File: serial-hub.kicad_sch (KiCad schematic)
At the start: 41 parts, among them J1 USB_C_Receptacle_USB2.0, J2 RJ45, J3 RJ45, J4 RJ45, J5 RJ45, U1 CH344, U2 MAX232, U3 AMS1117-3.3, U4 MAX232, U5 MAX232, U6 MAX232, Y1 8MHz

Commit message: init pcb design
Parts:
- removed C1: C, symbol Device:C
- added D1: 0, Diode_SMD:D_SOD-123, symbol Device:D
- added R3: 2, Resistor_SMD:R_0603_1608Metric, symbol Device:R
- added R4: 4.7k, Resistor_SMD:R_0402_1005Metric, symbol Device:R
- C1: renamed from C10; footprint (none) -> Capacitor_SMD:C_0603_1608Metric
- C10: renamed from C14; value 0.1uF -> 1uF; footprint (none) -> Capacitor_SMD:C_0402_1005Metric
- C11: renamed from C7; value 0.1uF -> 1uF; footprint (none) -> Capacitor_SMD:C_0402_1005Metric
- C12: renamed from C17; value 0.1uF -> 1uF; footprint (none) -> Capacitor_SMD:C_0402_1005Metric
- C13: renamed from C8; value 0.1uF -> 1uF; footprint (none) -> Capacitor_SMD:C_0402_1005Metric
- C14: renamed from C9; value 0.1uF -> 1uF; footprint (none) -> Capacitor_SMD:C_0402_1005Metric
- C15: renamed from C20; value 0.1uF -> 1uF; footprint (none) -> Capacitor_SMD:C_0402_1005Metric
- C16: renamed from C21; value 0.1uF -> 1uF; footprint (none) -> Capacitor_SMD:C_0402_1005Metric
- C17: renamed from C15; value 0.1uF -> 1uF; footprint (none) -> Capacitor_SMD:C_0402_1005Metric
- C18: renamed from C16; value 0.1uF -> 1uF; footprint (none) -> Capacitor_SMD:C_0402_1005Metric
- C19: renamed from C18; value 0.1uF -> 1uF; footprint (none) -> Capacitor_SMD:C_0402_1005Metric
- C2: footprint (none) -> Capacitor_SMD:C_0402_1005Metric
- C20: renamed from C19; value 0.1uF -> 1uF; footprint (none) -> Capacitor_SMD:C_0402_1005Metric
- C21: renamed from C22; value 0.1uF -> 1uF; footprint (none) -> Capacitor_SMD:C_0402_1005Metric
- C22: renamed from C23; value 0.1uF -> 1uF; footprint (none) -> Capacitor_SMD:C_0402_1005Metric
- C23: renamed from C24; value 0.1uF -> 1uF; footprint (none) -> Capacitor_SMD:C_0402_1005Metric
- C24: renamed from C25; value 0.1uF -> 1uF; footprint (none) -> Capacitor_SMD:C_0402_1005Metric
- C3: renamed from C11; footprint (none) -> Capacitor_SMD:C_0402_1005Metric
- C4: renamed from C12; footprint (none) -> Capacitor_SMD:C_0402_1005Metric
- C5: renamed from C13; value 10uF -> 22uF; footprint (none) -> Capacitor_SMD:C_0603_1608Metric
- C6: renamed from C3; footprint (none) -> Capacitor_SMD:C_0402_1005Metric
- C7: renamed from C4; footprint (none) -> Capacitor_SMD:C_0402_1005Metric
- C8: renamed from C5; value C -> 0.1uF; footprint (none) -> Capacitor_SMD:C_0402_1005Metric
- C9: renamed from C6; value 0.1uF -> 1uF; footprint (none) -> Capacitor_SMD:C_0402_1005Metric
- R1: renamed from R2; footprint (none) -> Resistor_SMD:R_0402_1005Metric
- R2: renamed from R3; footprint (none) -> Resistor_SMD:R_0402_1005Metric
- R5: renamed from R1; footprint (none) -> Resistor_SMD:R_0402_1005Metric
- R6: renamed from R4; footprint (none) -> Resistor_SMD:R_0402_1005Metric
- U3: renamed from U2; footprint (none) -> Package_SO:SOIC-16_3.9x9.9mm_P1.27mm
- U4, U5, U6: footprint (none) -> Package_SO:SOIC-16_3.9x9.9mm_P1.27mm
- Y1: footprint (none) -> Crystal:Crystal_SMD_5032-2Pin_5.0x3.2mm
- renumbered U3 to U2
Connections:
- net +3.3V: now also R3.1; no longer C5.1
- net C0_RX: no longer U1.13 (RXD1)
- net C1_RX: now also U1.13 (RXD1)
- net GND: now also U2.1 (GND), R4.2
- net VBUS: now also D1.1 (K); no longer J1.A4 (VBUS), J1.A9 (VBUS), J1.B4 (VBUS), J1.B9 (VBUS)
- net RTS3: now reaches U1.45 (RTS3/GPIO7)
- net RTS3: now also R4.1
- new net: D1.2 (A), J1.A4 (VBUS), J1.A9 (VBUS), J1.B4 (VBUS), J1.B9 (VBUS)
- new net: C5.1, R3.2
- no-connect marks 18 -> 17
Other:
- moved on the sheet: C10, C11, C12, C13, C14, C15, C16, C17, C18, C19, C20, C21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

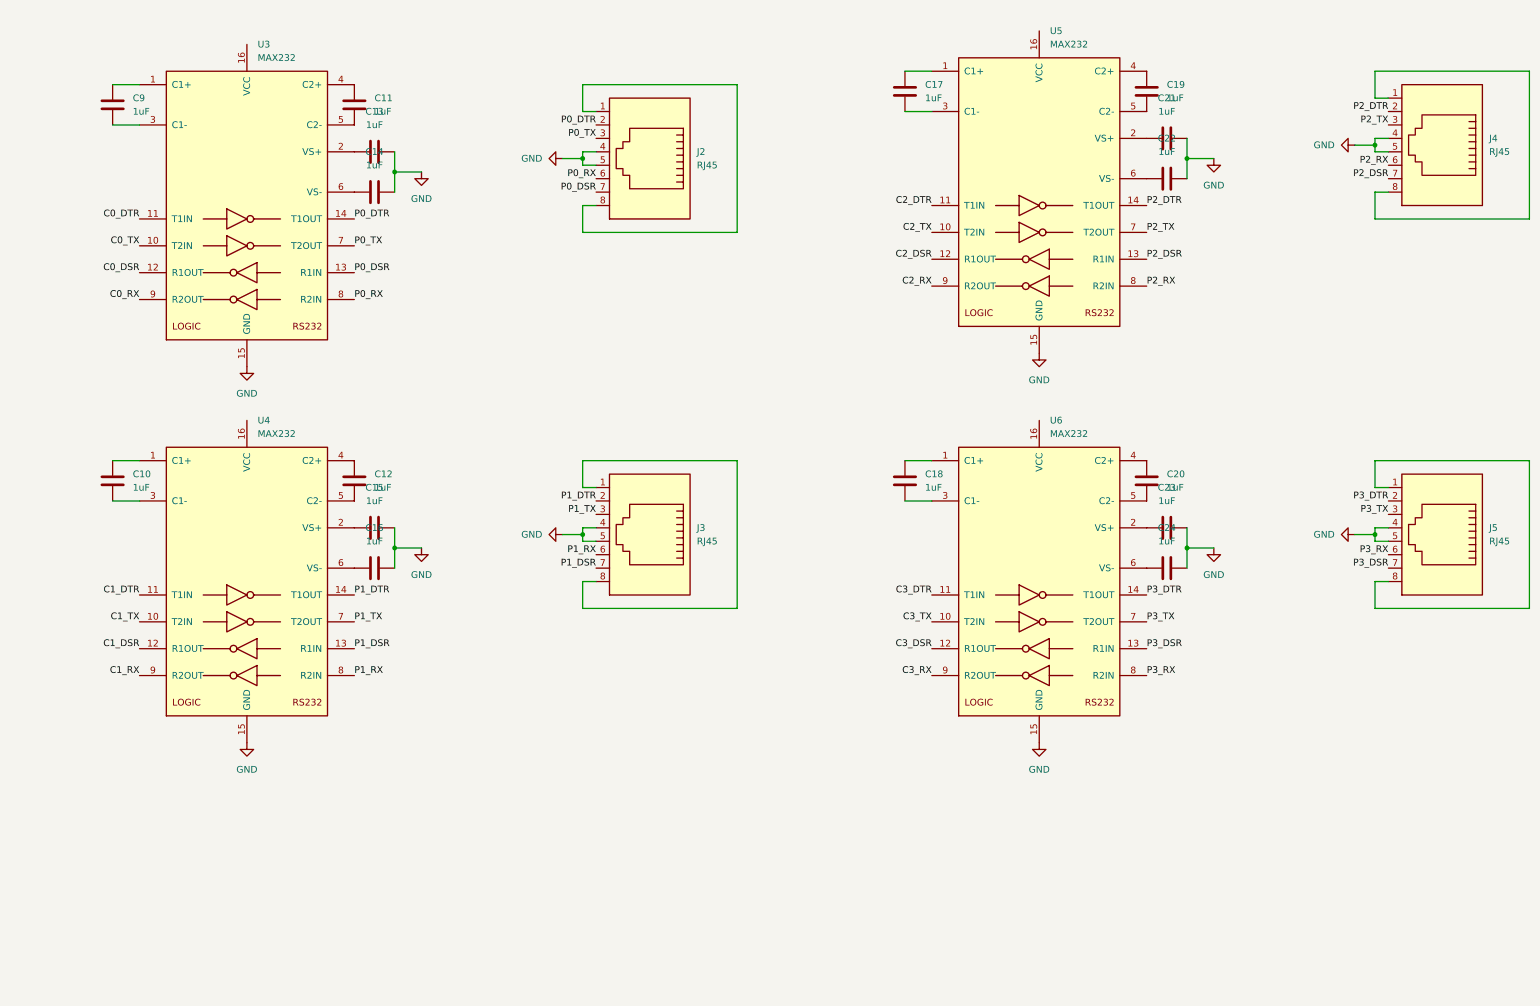
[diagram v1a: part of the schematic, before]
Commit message: fix max232 caps
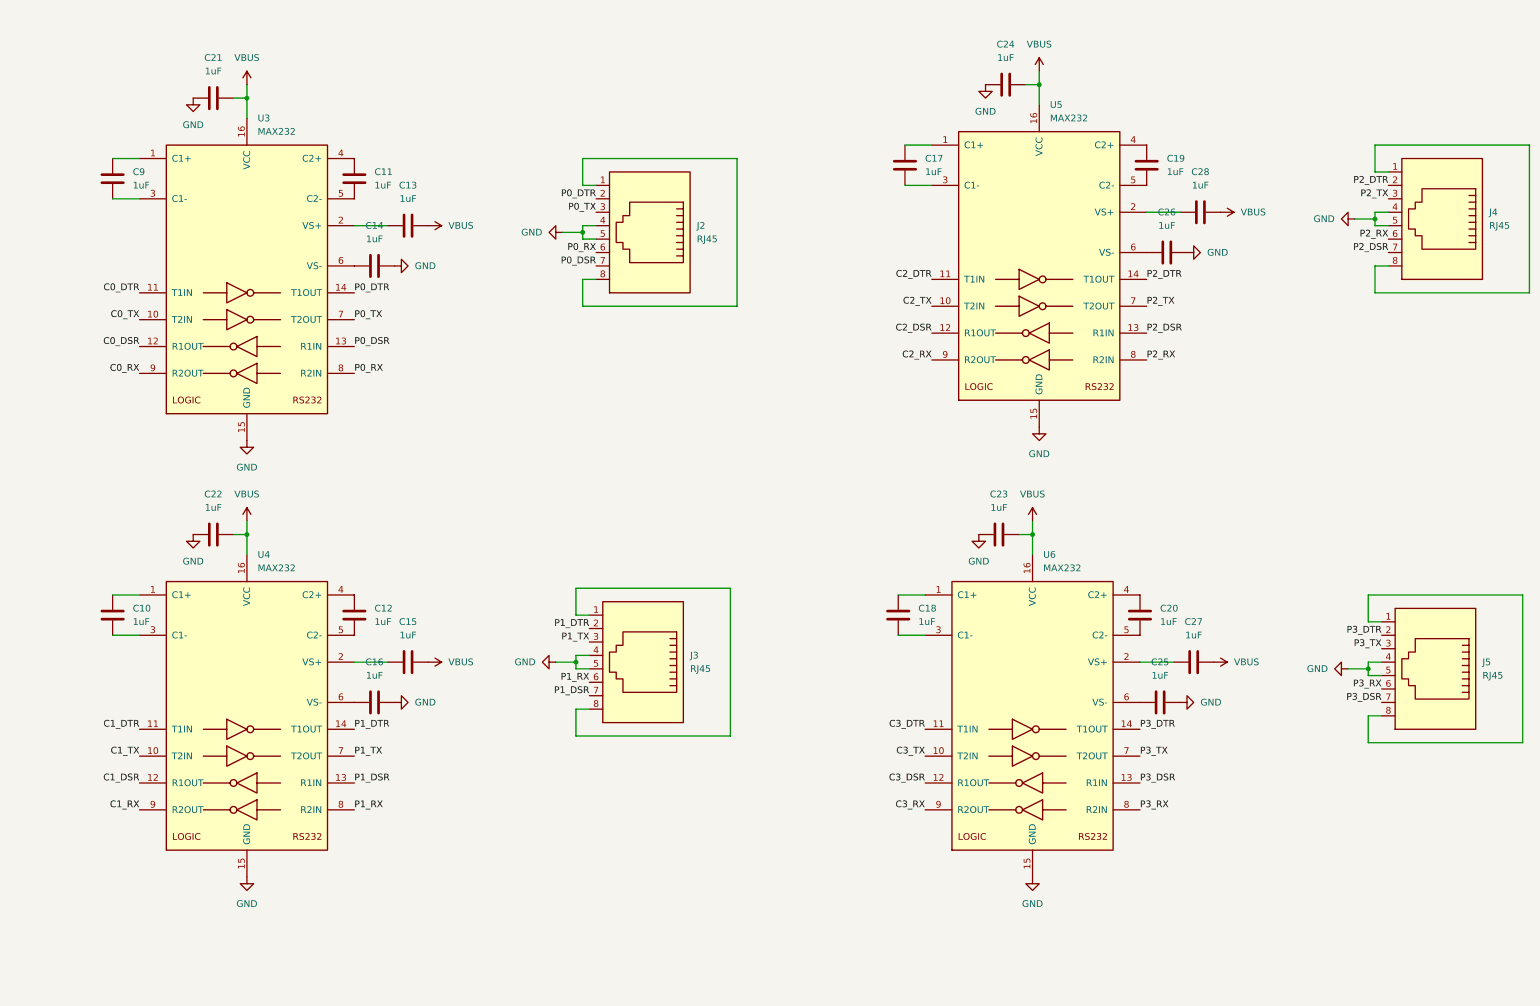
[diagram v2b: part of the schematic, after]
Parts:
- added C25, C26, C27, C28: 1uF, Capacitor_SMD:C_0402_1005Metric, symbol Device:C
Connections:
- net GND: now also C21.1, C22.1, C23.1, C24.1, C25.2, C26.2; no longer C13.2, C15.2, C21.2, C22.2, C23.2, C24.2
- net VBUS: now also C13.2, C15.2, C21.2, C22.2, C23.2, C24.2, U3.16 (VCC), U4.16 (VCC), U5.16 (VCC), U6.16 (VCC), C27.2, C28.2
- net at U5.2 (VS+): now also C28.1; no longer C21.1
- net at U6.2 (VS+): now also C27.1; no longer C23.1
- net at U6.6 (VS-): now also C25.1; no longer C24.1
- net at U5.6 (VS-): now also C26.1; no longer C22.1
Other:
- moved on the sheet: C10, C11, C12, C13, C14, C15, C16, C17, C18, C19, C20, C9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

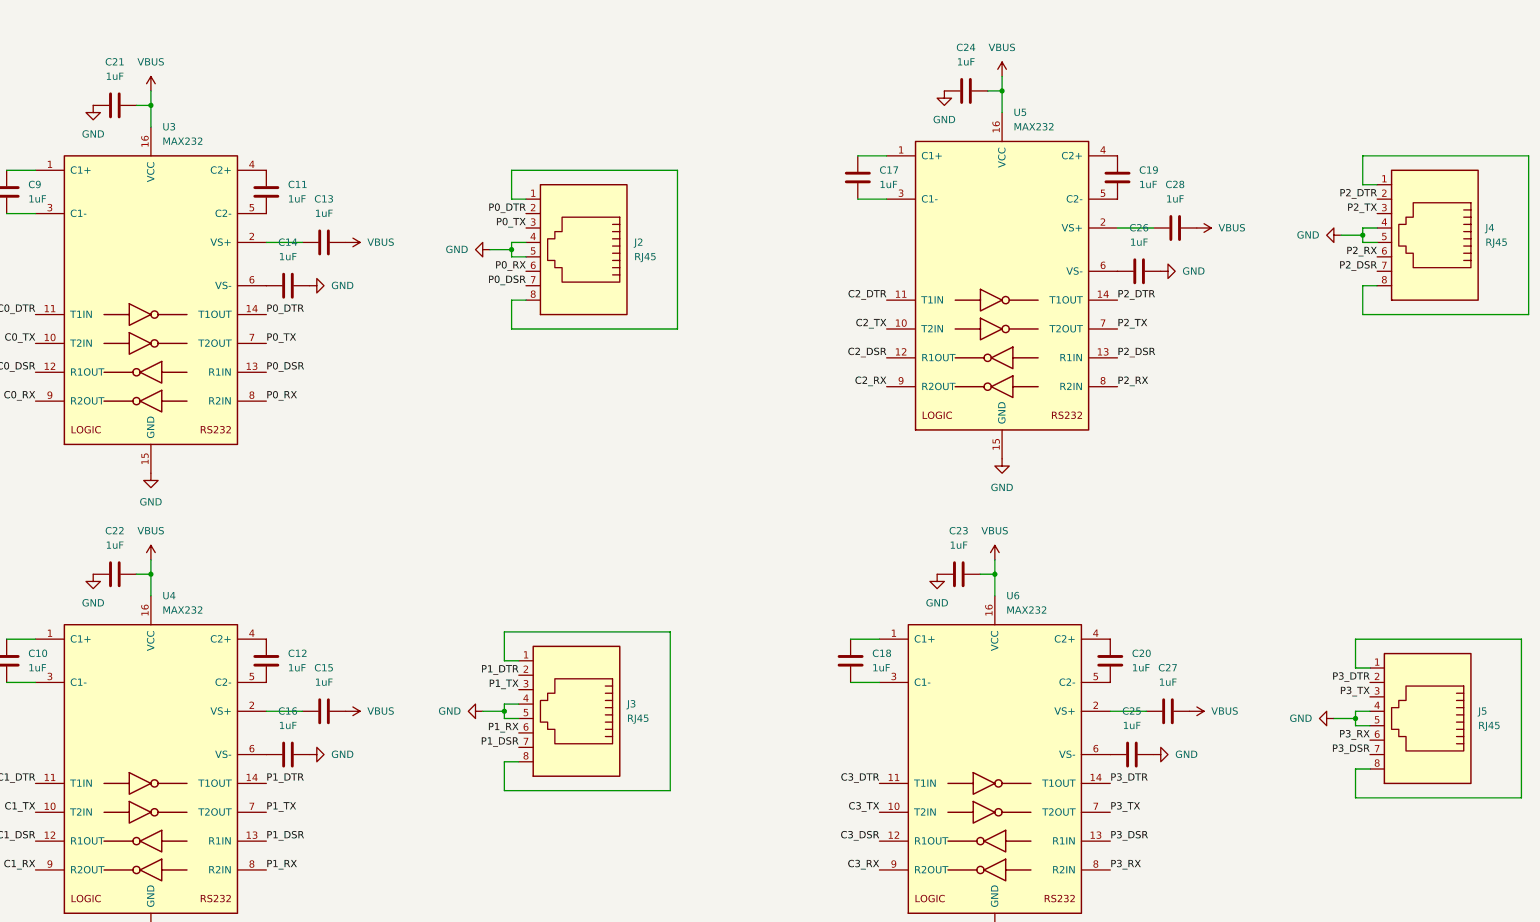
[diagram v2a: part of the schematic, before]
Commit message: update schematic
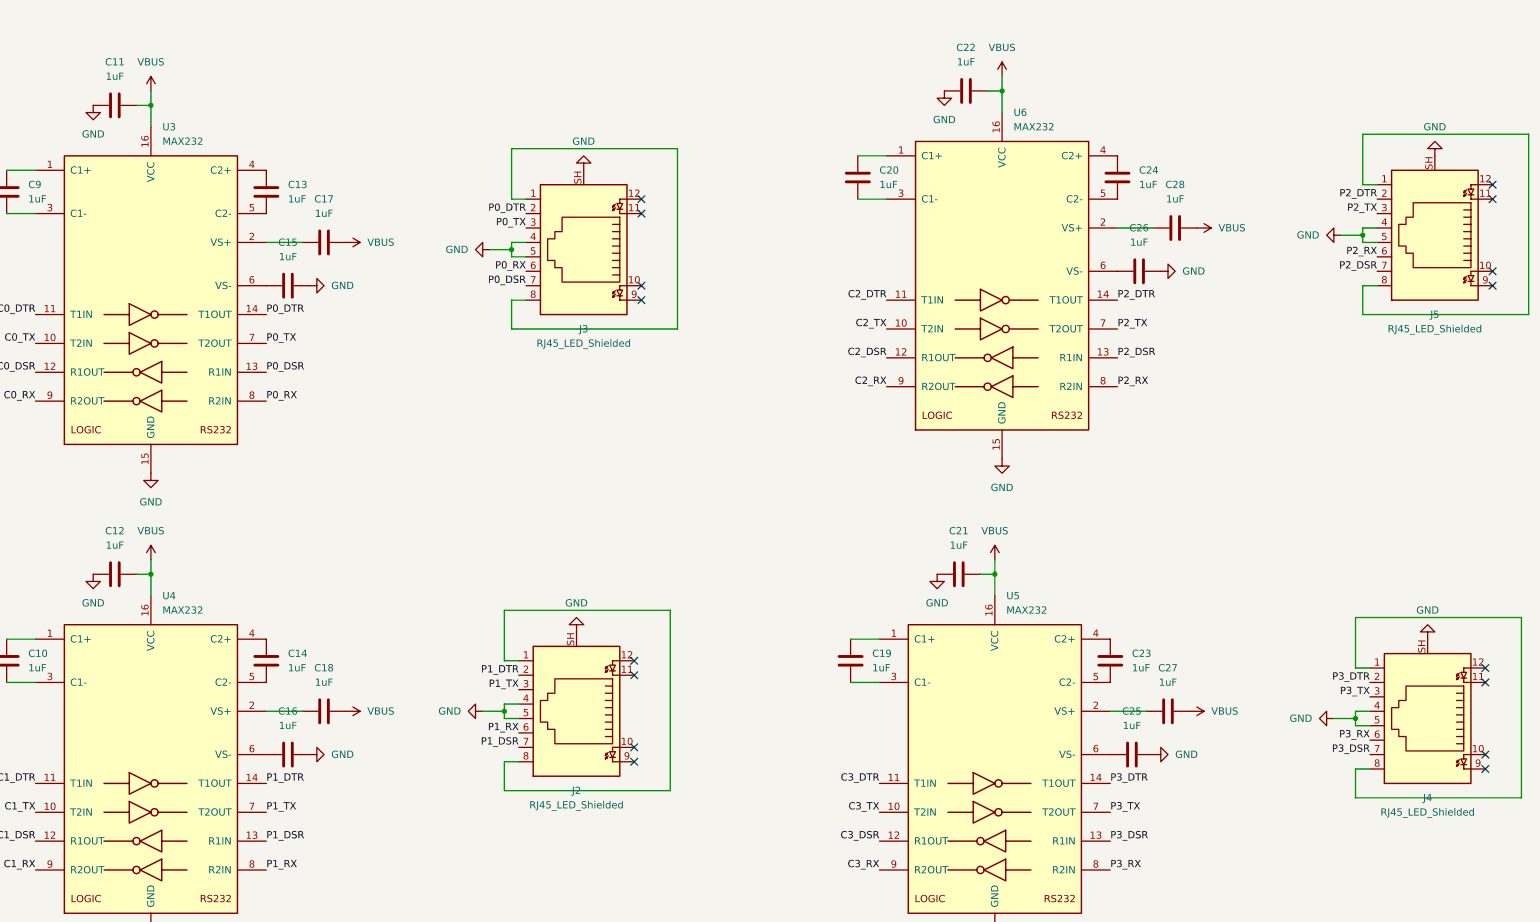
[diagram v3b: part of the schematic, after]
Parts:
- removed J2, J3, J4, J5: RJ45, Connector_RJ:RJ45_Amphenol_RJHSE538X, symbol Connector:RJ45
- added J2, J3, J4, J5: RJ45_LED_Shielded, symbol Connector:RJ45_LED_Shielded
- renumbered C21 to C11, C22 to C12, C11 to C13, C12 to C14, C14 to C15, C13 to C17, C15 to C18, C18 to C19, C17 to C20, C23 to C21, C24 to C22, C20 to C23, C19 to C24, U6 to U5, U5 to U6
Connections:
- net GND: now also J2.4, J2.5, J2.SH, J3.4, J3.5, J3.SH, J4.4, J4.5, J4.SH, J5.4, J5.5, J5.SH
- net P0_DSR: now also J3.7
- net P0_DTR: now also J3.2
- net P0_RX: now also J3.6
- net P0_TX: now also J3.3
- net P1_DSR: now also J2.7
- net P1_DTR: now also J2.2
- net P1_RX: now also J2.6
- net P1_TX: now also J2.3
- net P2_DSR: now also J5.7
- net P2_DTR: now also J5.2
- net P2_RX: now also J5.6
- net P2_TX: now also J5.3
- net P3_DSR: now also J4.7
- net P3_DTR: now also J4.2
- net P3_RX: now also J4.6
- net P3_TX: now also J4.3
- new net: J5.1, J5.8
- new net: J4.1, J4.8
- new net: J2.1, J2.8
- new net: J3.1, J3.8
- no-connect marks 17 -> 33

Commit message: update sch
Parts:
- C10, C11, C12, C13, C14, C15, C16, C17, C18, C19, C2, C20, C21, C22, C23, C24, C25, C26, C27, C28, C3, C4, C8, C9: footprint Capacitor_SMD:C_0402_1005Metric -> Capacitor_SMD:C_0603_1608Metric
- C5: footprint Capacitor_SMD:C_0603_1608Metric -> Capacitor_SMD:C_0805_2012Metric
- C6, C7: footprint Capacitor_SMD:C_0402_1005Metric -> Capacitor_SMD:C_0805_2012Metric
- J2, J3, J4, J5: footprint (none) -> Connector_RJ:RJ45_Hanrun_HR911105A
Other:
- moved on the sheet: C8, R6

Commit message: update PCB
Signed-off-by: David Bauer <mail@david-bauer.net>
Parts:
- C1: LCSC (none) -> C96446
- C10, C11, C12, C13, C14, C15, C16, C17, C18, C19, C20, C21, C22, C23, C24, C25, C26, C27, C28, C9: LCSC (none) -> C15849
- C2, C3, C4, C8: LCSC (none) -> C14663
- C5: LCSC (none) -> C45783
- C6, C7: footprint Capacitor_SMD:C_0805_2012Metric -> Capacitor_SMD:C_0402_1005Metric; LCSC (none) -> C1555
- D1: LCSC (none) -> C8598
- J1: LCSC (none) -> C963413
- J2, J3, J4, J5: LCSC (none) -> C12074
- R1, R2: LCSC (none) -> C17606
- R3: LCSC (none) -> C22977
- R4, R5, R6: LCSC (none) -> C25900
- U1: LCSC (none) -> C2988084
- U2: LCSC (none) -> C6186
- U3, U4, U5, U6: LCSC (none) -> C26860
- Y1: LCSC (none) -> C115962
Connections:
- net C0_DSR: no longer names the net of U3.12 (R1OUT)
- net C0_DSR: no longer U1.29 (DSR0/GPIO14)
- net C0_DTR: no longer names the net of U3.11 (T1IN)
- net C0_DTR: no longer U1.39 (DTR0/TNOW0/GPIO8)
- net C1_DSR: no longer names the net of U4.12 (R1OUT)
- net C1_DSR: no longer U1.17 (DSR1)
- net C1_DTR: no longer names the net of U4.11 (T1IN)
- net C1_DTR: no longer U1.18 (DTR1/TNOW1/GPIO9)
- net C2_DSR: no longer names the net of U1.2 (DSR2)
- net C2_DSR: no longer U6.12 (R1OUT)
- net C2_DTR: no longer names the net of U1.19 (DTR2/TNOS2/GPIO10)
- net C2_DTR: no longer U6.11 (T1IN)
- net C3_DSR: no longer names the net of U5.12 (R1OUT)
- net C3_DSR: no longer U1.16 (DSR3/RX_S)
- net C3_DTR: no longer names the net of U5.11 (T1IN)
- net C3_DTR: no longer U1.34 (DTR3/TNOW3/GPIO11)
- net P0_DSR: no longer names the net of U3.13 (R1IN)
- net P0_DSR: no longer J3.7
- net P0_DTR: no longer names the net of U3.14 (T1OUT)
- net P0_DTR: no longer J3.2
- net P1_DSR: no longer names the net of U4.13 (R1IN)
- net P1_DSR: no longer J2.7
- net P1_DTR: no longer names the net of U4.14 (T1OUT)
- net P1_DTR: no longer J2.2
- net P2_DSR: no longer names the net of J5.7
- net P2_DSR: now also J5.2; no longer U6.13 (R1IN)
- net P2_DTR: no longer names the net of U6.14 (T1OUT)
- net P2_DTR: no longer J5.2
- net P3_DSR: no longer names the net of U5.13 (R1IN)
- net P3_DSR: no longer J4.7
- net P3_DTR: no longer names the net of U5.14 (T1OUT)
- net P3_DTR: no longer J4.2
- new net: J4.2, J4.7
- new net: J2.2, J2.7
- new net: J3.2, J3.7
- no-connect marks 33 -> 56

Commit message: fix USB-C part number
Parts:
- J1: LCSC C963413 -> C2988369
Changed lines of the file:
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@@
       (effects (font (size 1.27 1.27)) hide)
     )
-    (property "LCSC" "C963413" (id 4) (at 30.48 143.51 0)
+    (property "LCSC" "C2988369" (id 4) (at 30.48 143.51 0)
       (effects (font (size 1.27 1.27)) hide)
     )

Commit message: add test-pins for UART
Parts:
- added J2: Conn_01x04_Male, Connector_PinHeader_2.54mm:PinHeader_1x04_P2.54mm_Vertical, symbol Connector:Conn_01x04_Male
- added J3, J4, J7, J8: Conn_01x03_Male, Connector_PinHeader_2.54mm:PinHeader_1x03_P2.54mm_Vertical, symbol Connector:Conn_01x03_Male
- renumbered J5 to J10, J2 to J5, J3 to J6, J4 to J9
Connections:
- net C0_RX: now also J3.2 (Pin_2)
- net C0_TX: now also J3.3 (Pin_3)
- net C1_RX: now also J4.2 (Pin_2)
- net C1_TX: now also J4.3 (Pin_3)
- net C2_RX: now also J7.2 (Pin_2)
- net C2_TX: now also J7.3 (Pin_3)
- net C3_RX: now also J8.2 (Pin_2)
- net C3_TX: now also J8.3 (Pin_3)
- net GND: now also J2.4 (Pin_4), J3.1 (Pin_1), J4.1 (Pin_1), J7.1 (Pin_1), J8.1 (Pin_1)
- net HOST_DM: now also J2.2 (Pin_2)
- net HOST_DP: now also J2.3 (Pin_3)
- net VCC: now reaches D1.2 (A), J1.A4 (VBUS), J1.A9 (VBUS), J1.B4 (VBUS), J1.B9 (VBUS)
- net VCC: now also J2.1 (Pin_1)
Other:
- moved on the sheet: D1

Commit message: switch USB-C / add CH344 input caps
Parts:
- added C4, C5, C6: 0.1uF, Capacitor_SMD:C_0603_1608Metric, symbol Device:C
- J1: footprint Connector_USB:USB_C_Receptacle_G-Switch_GT-USB-7010ASV -> Connector_USB:USB_C_Receptacle_XKB_U262-16XN-4BVC11
- renumbered C7 to C10, C8 to C11, C9 to C12, C10 to C13, C11 to C14, C12 to C15, C13 to C16, C14 to C17, C15 to C18, C16 to C19, C17 to C20, C18 to C21, C19 to C22, C20 to C23, C21 to C24, C22 to C25, C23 to C26, C24 to C27, C25 to C28, C26 to C29, C27 to C30, C28 to C31, C4 to C7, C5 to C8, C6 to C9
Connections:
- net +3.3V: now also C4.1, C5.1, C6.1
- net GND: now also C4.2, C5.2, C6.2
